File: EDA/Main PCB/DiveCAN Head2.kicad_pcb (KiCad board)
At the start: 4 copper layers, 97.1 x 26 mm, 157 parts, among them J1 Micro_SD_Card_Det1, J2 Analog Connection, J3 Digital Connection, J4 CAN Connection, J5 JTAG, Q1 SI2302, Q2 SI2302, Q3 2N7000, SW1 RST, SW2 RST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

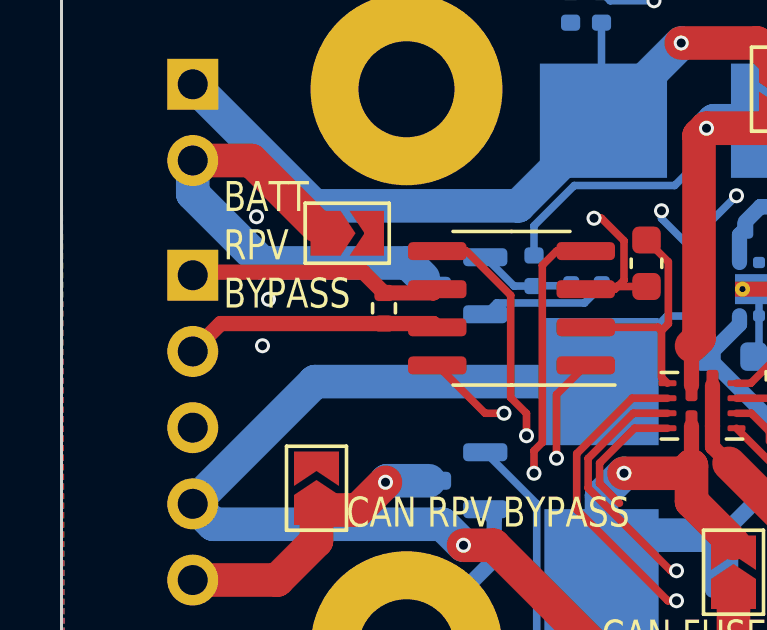
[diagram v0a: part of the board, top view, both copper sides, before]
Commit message: switch R35 to JLC basic on Main and Jr boards
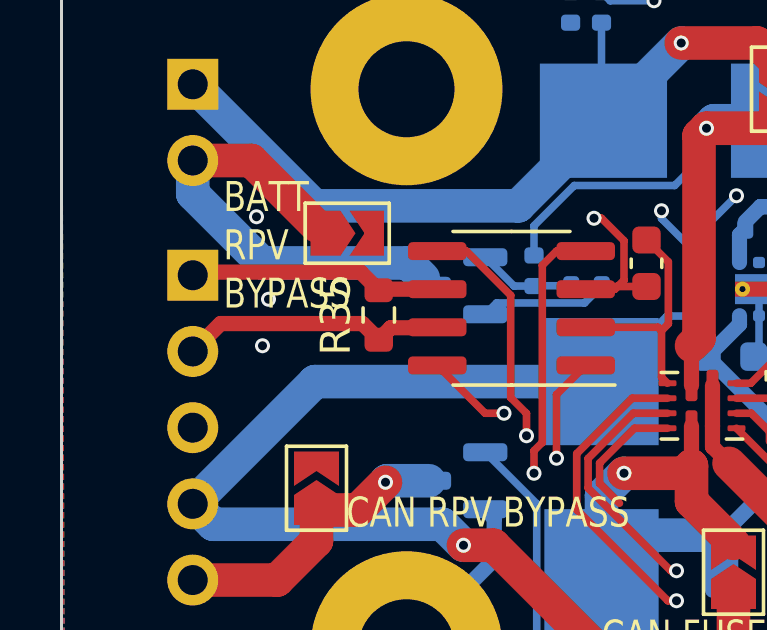
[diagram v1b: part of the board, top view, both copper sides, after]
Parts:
- R35: footprint Resistor_SMD:R_0402_1005Metric -> Resistor_SMD:R_0603_1608Metric
- moved R35 0.29 mm to (89.1, 82.7)
